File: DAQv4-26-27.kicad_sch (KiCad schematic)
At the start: 1 part, among them U1 STM32H745IITx

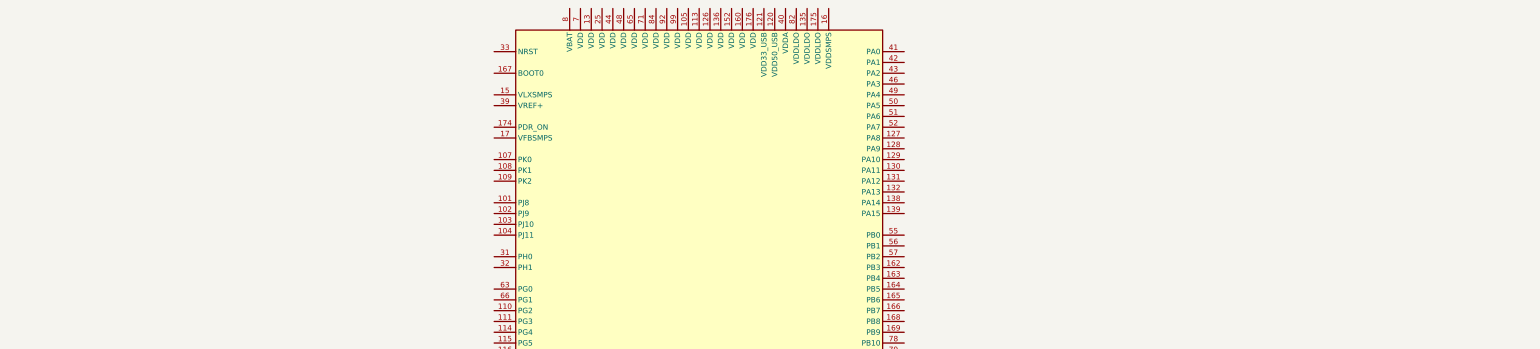
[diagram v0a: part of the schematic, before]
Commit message: added symbol for adc
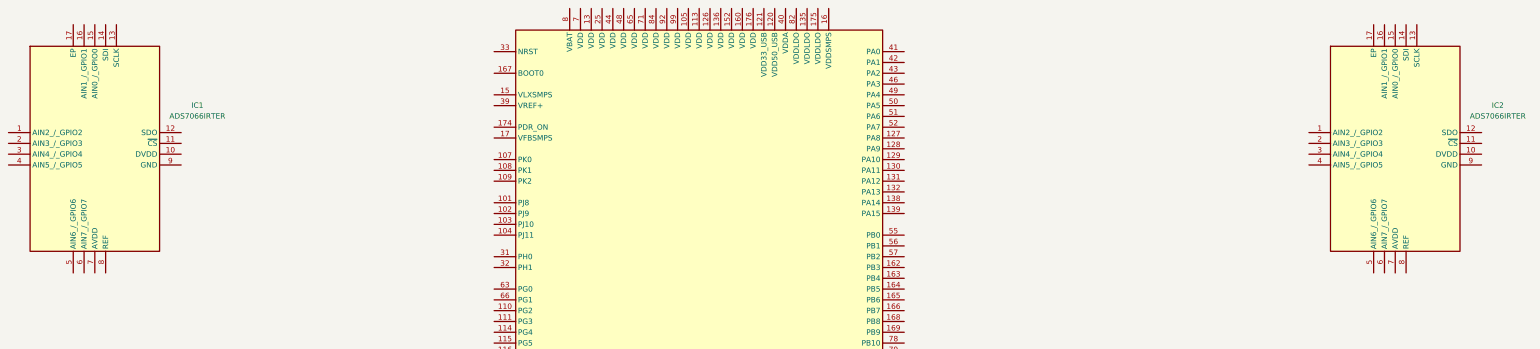
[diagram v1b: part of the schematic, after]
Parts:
- added IC1, IC2: ADS7066IRTER, QFN50P300X300X80-17N-D, symbol ADS7066IRTER:ADS7066IRTER

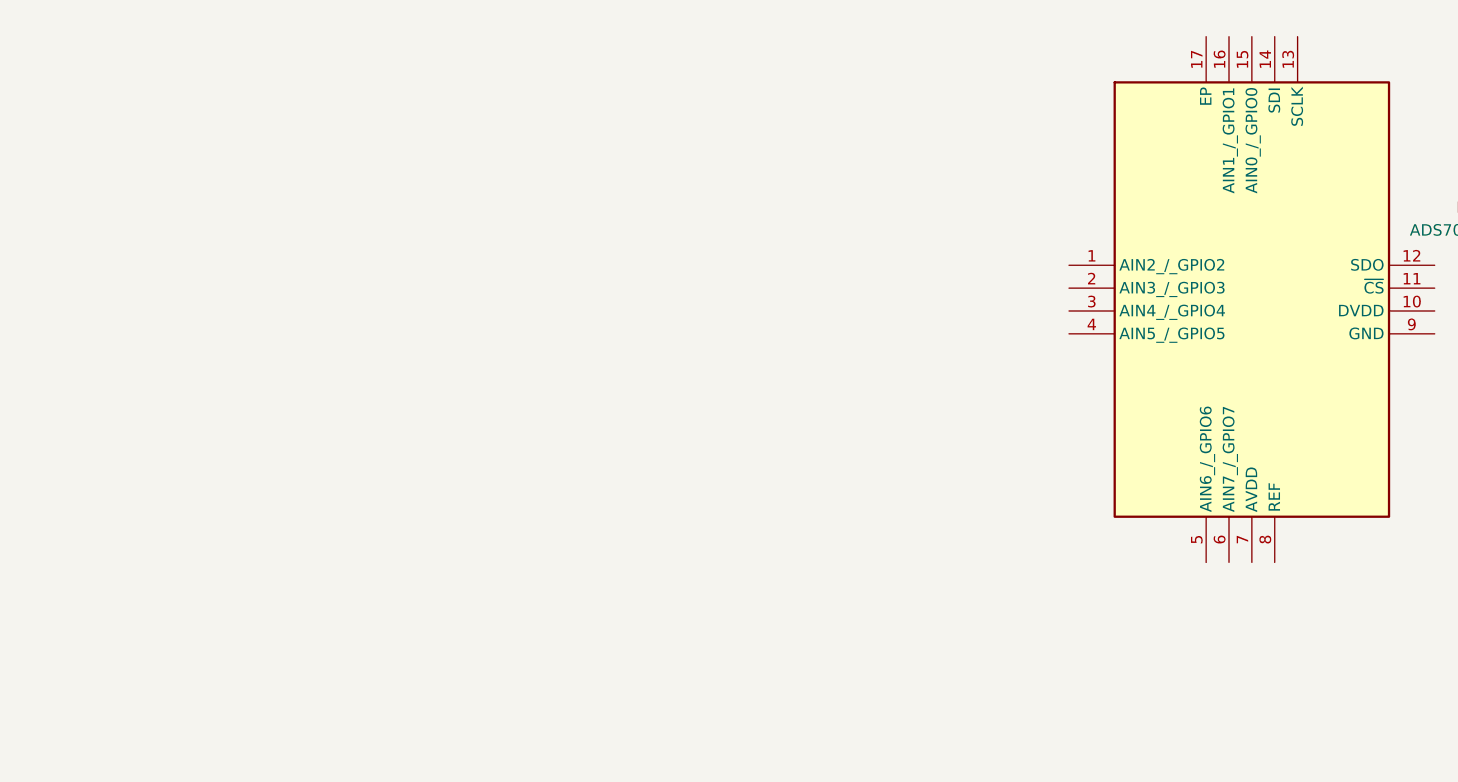
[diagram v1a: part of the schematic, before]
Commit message: Work done on adding a amp to the thermocouple
ad8494, using the basic connection as shown in the datasheet
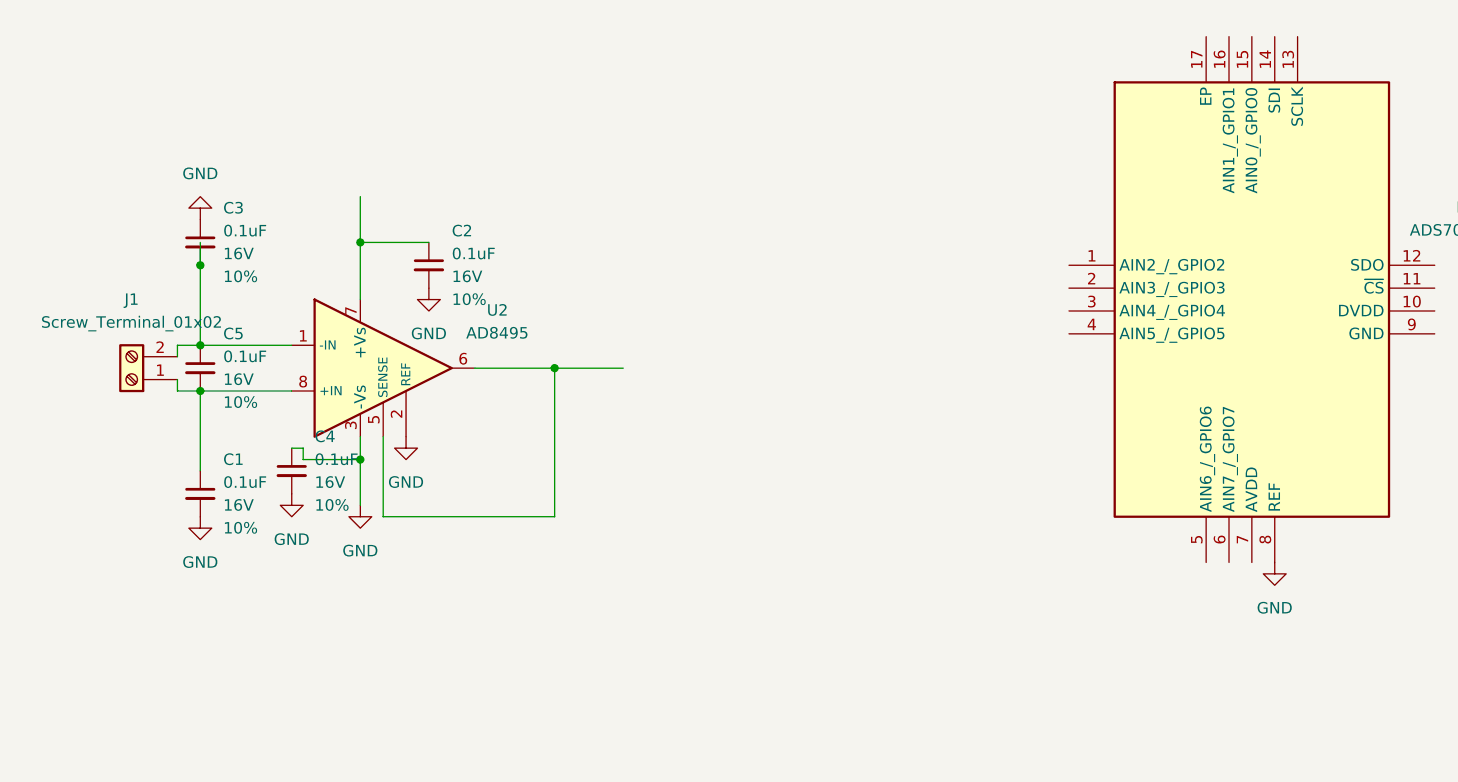
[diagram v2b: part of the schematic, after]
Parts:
- added C1, C2, C3, C4, C5: 0.1uF, PCM_SparkFun-Capacitor:C_0402_1005Metric, symbol PCM_SparkFun-Capacitor:0.1uF_0402_16V_10%
- added J1: Screw_Terminal_01x02, symbol Connector:Screw_Terminal_01x02
- added U2: AD8495, Package_SO:MSOP-8_3x3mm_P0.65mm, symbol Sensor_Temperature:AD8495
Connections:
- net GND: now reaches IC1.8 (REF)
- net GND: now also C1.2, C2.2, C3.1, C4.1, C4.2, U2.2 (REF), U2.3 (-Vs)
- new net: C3.2, C5.1, J1.2 (Pin_2), U2.1 (-IN)
- new net: U2.5 (SENSE), U2.6
- new net: C2.1, U2.7 (+Vs)
- new net: C1.1, C5.2, J1.1 (Pin_1), U2.8 (+IN)
